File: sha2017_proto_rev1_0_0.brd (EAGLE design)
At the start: 95 x 46 mm, 1 part

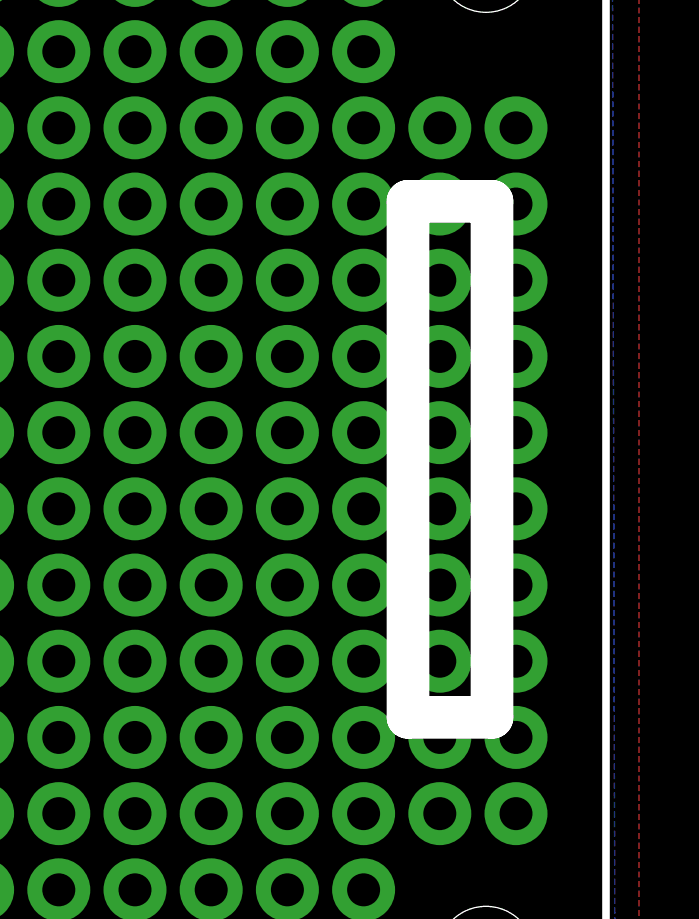
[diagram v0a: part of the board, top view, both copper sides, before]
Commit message: removed milling layer
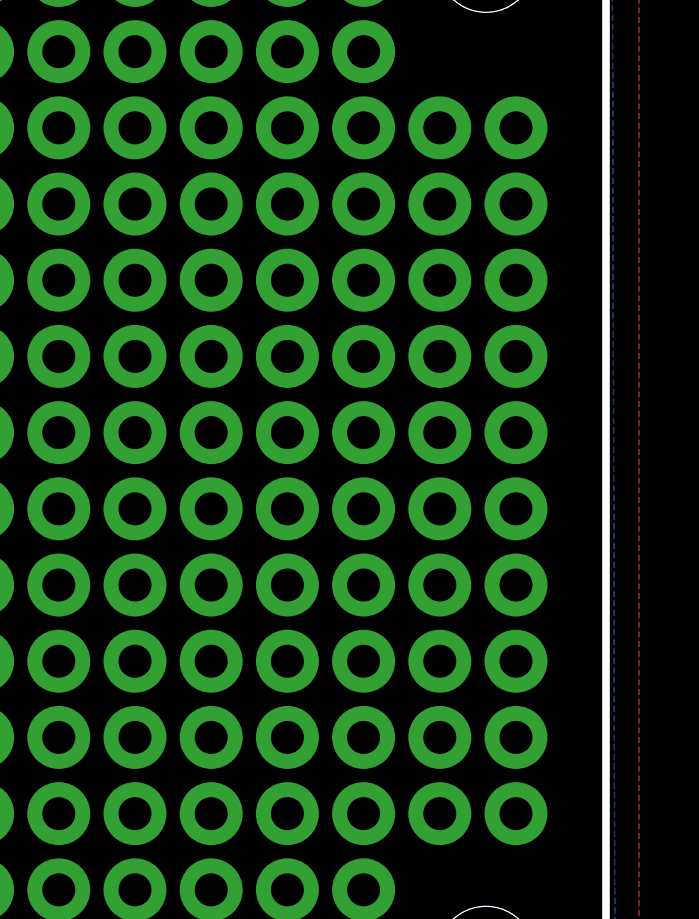
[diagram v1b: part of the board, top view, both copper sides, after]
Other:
- outline, holes or cut-outs redrawn
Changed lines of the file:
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@@
 <layer number="25" name="tNames" color="7" fill="1" visible="yes" active="yes"/>
 <layer number="26" name="bNames" color="7" fill="1" visible="yes" active="yes"/>
-<layer number="27" name="tValues" color="7" fill="1" visible="no" active="yes"/>
-<layer number="28" name="bValues" color="7" fill="1" visible="no" active="yes"/>
+<layer number="27" name="tValues" color="7" fill="1" visible="yes" active="yes"/>
+<layer number="28" name="bValues" color="7" fill="1" visible="yes" active="yes"/>
 <layer number="29" name="tStop" color="7" fill="3" visible="yes" active="yes"/>
 <layer number="30" name="bStop" color="7" fill="6" visible="yes" active="yes"/>
-<layer number="31" name="tCream" color="7" fill="4" visible="no" active="yes"/>
-<layer number="32" name="bCream" color="7" fill="5" visible="no" active="yes"/>
-<layer number="33" name="tFinish" color="6" fill="3" visible="no" active="yes"/>
-<layer number="34" name="bFinish" color="6" fill="6" visible="no" active="yes"/>
-<layer number="35" name="tGlue" color="7" fill="4" visible="no" active="yes"/>
-<layer number="36" name="bGlue" color="7" fill="5" visible="no" active="yes"/>
-<layer number="37" name="tTest" color="7" fill="1" visible="no" active="yes"/>
-<layer number="38" name="bTest" color="7" fill="1" visible="no" active="yes"/>
-<layer number="39" name="tKeepout" color="4" fill="11" visible="no" active="yes"/>
-<layer number="40" name="bKeepout" color="1" fill="11" visible="no" active="yes"/>
-<layer number="41" name="tRestrict" color="4" fill="10" visible="no" active="yes"/>
-<layer number="42" name="bRestrict" color="1" fill="10" visible="no" active="yes"/>
-<layer number="43" name="vRestrict" color="2" fill="10" visible="no" active="yes"/>
-<layer number="44" name="Drills" color="7" fill="1" visible="no" active="yes"/>
+<layer number="31" name="tCream" color="7" fill="4" visible="yes" active="yes"/>
+<layer number="32" name="bCream" color="7" fill="5" visible="yes" active="yes"/>
+<layer number="33" name="tFinish" color="6" fill="3" visible="yes" active="yes"/>
+<layer number="34" name="bFinish" color="6" fill="6" visible="yes" active="yes"/>
+<layer number="35" name="tGlue" color="7" fill="4" visible="yes" active="yes"/>
+<layer number="36" name="bGlue" color="7" fill="5" visible="yes" active="yes"/>
+<layer number="37" name="tTest" color="7" fill="1" visible="yes" active="yes"/>
+<layer number="38" name="bTest" color="7" fill="1" visible="yes" active="yes"/>
+<layer number="39" name="tKeepout" color="4" fill="11" visible="yes" active="yes"/>
+<layer number="40" name="bKeepout" color="1" fill="11" visible="yes" active="yes"/>
+<layer number="41" name="tRestrict" color="4" fill="10" visible="yes" active="yes"/>
+<layer number="42" name="bRestrict" color="1" fill="10" visible="yes" active="yes"/>
+<layer number="43" name="vRestrict" color="2" fill="10" visible="yes" active="yes"/>
+<layer number="44" name="Drills" color="7" fill="1" visible="yes" active="yes"/>
 <layer number="45" name="Holes" color="7" fill="1" visible="yes" active="yes"/>
-<layer number="46" name="Milling" color="3" fill="1" visible="no" active="yes"/>
-<layer number="47" name="Measures" color="7" fill="1" visible="no" active="yes"/>
-<layer number="48" name="Document" color="7" fill="1" visible="no" active="yes"/>
-<layer number="49" name="Reference" color="7" fill="1" visible="no" active="yes"/>
+<layer number="46" name="Milling" color="3" fill="1" visible="yes" active="yes"/>
+<layer number="47" name="Measures" color="7" fill="1" visible="yes" active="yes"/>
+<layer number="48" name="Document" color="7" fill="1" visible="yes" active="yes"/>
+<layer number="49" name="Reference" color="7" fill="1" visible="yes" active="yes"/>
 <layer number="50" name="dxf" color="7" fill="1" visible="no" active="no"/>
-<layer number="51" name="tDocu" color="7" fill="1" visible="no" active="yes"/>
-<layer number="52" name="bDocu" color="7" fill="1" visible="no" active="yes"/>
+<layer number="51" name="tDocu" color="7" fill="1" visible="yes" active="yes"/>
+<layer number="52" name="bDocu" color="7" fill="1" visible="yes" active="yes"/>
 <layer number="53" name="tGND_GNDA" color="7" fill="9" visible="no" active="no"/>
 <layer number="54" name="bGND_GNDA" color="1" fill="9" visible="no" active="no"/>
@@
 <layer number="60" name="bCarbon" color="7" fill="1" visible="no" active="no"/>
 <layer number="61" name="stand" color="7" fill="1" visible="no" active="no"/>
-<layer number="90" name="Modules" color="5" fill="1" visible="no" active="yes"/>
+<layer number="90" name="Modules" color="5" fill="1" visible="yes" active="yes"/>
 <layer number="91" name="Nets" color="2" fill="1" visible="no" active="no"/>
 <layer number="92" name="Busses" color="1" fill="1" visible="no" active="no"/>
@@
 <layer number="99" name="SpiceOrder" color="7" fill="1" visible="no" active="no"/>
 <layer number="100" name="Muster" color="7" fill="1" visible="no" active="no"/>
-<layer number="101" name="Patch_Top" color="12" fill="4" visible="no" active="yes"/>
-<layer number="102" name="Vscore" color="7" fill="1" visible="no" active="yes"/>
-<layer number="103" name="tMap" color="7" fill="1" visible="no" active="yes"/>
-<layer number="104" name="Name" color="16" fill="1" visible="no" active="yes"/>
-<layer number="105" name="tPlate" color="7" fill="1" visible="no" active="yes"/>
-<layer number="106" name="bPlate" color="7" fill="1" visible="no" active="yes"/>
-<layer number="107" name="Crop" color="7" fill="1" visible="no" active="yes"/>
-<layer number="108" name="tplace-old" color="10" fill="1" visible="no" active="yes"/>
-<layer number="109" name="ref-old" color="11" fill="1" visible="no" active="yes"/>
-<layer number="110" name="fp0" color="7" fill="1" visible="no" active="yes"/>
-<layer number="111" name="LPC17xx" color="7" fill="1" visible="no" active="yes"/>
-<layer number="112" name="tSilk" color="7" fill="1" visible="no" active="yes"/>
+<layer number="101" name="Patch_Top" color="12" fill="4" visible="yes" active="yes"/>
+<layer number="102" name="Vscore" color="7" fill="1" visible="yes" active="yes"/>
+<layer number="103" name="tMap" color="7" fill="1" visible="yes" active="yes"/>
+<layer number="104" name="Name" color="16" fill="1" visible="yes" active="yes"/>
+<layer number="105" name="tPlate" color="7" fill="1" visible="yes" active="yes"/>
+<layer number="106" name="bPlate" color="7" fill="1" visible="yes" active="yes"/>
+<layer number="107" name="Crop" color="7" fill="1" visible="yes" active="yes"/>
+<layer number="108" name="tplace-old" color="10" fill="1" visible="yes" active="yes"/>
+<layer number="109" name="ref-old" color="11" fill="1" visible="yes" active="yes"/>
+<layer number="110" name="fp0" color="7" fill="1" visible="yes" active="yes"/>
+<layer number="111" name="LPC17xx" color="7" fill="1" visible="yes" active="yes"/>
+<layer number="112" name="tSilk" color="7" fill="1" visible="yes" active="yes"/>
 <layer number="113" name="IDFDebug" color="7" fill="1" visible="no" active="yes"/>
 <layer number="116" name="Patch_BOT" color="9" fill="4" visible="no" active="yes"/>
@@
 <wire x1="95" y1="43" x2="95" y2="81" width="0.254" layer="20"/>
 <wire x1="95" y1="81" x2="91" y2="85" width="0.254" layer="20" curve="90"/>
-<wire x1="91.2" y1="67.1" x2="91.2" y2="49.9" width="1.4224" layer="46"/>
-<wire x1="91.2" y1="49.9" x2="88.4" y2="49.9" width="1.4224" layer="46"/>
-<wire x1="88.4" y1="49.9" x2="88.4" y2="67.1" width="1.4224" layer="46"/>
-<wire x1="88.4" y1="67.1" x2="91.2" y2="67.1" width="1.4224" layer="46"/>
 <hole x="3" y="57" drill="3.2"/>
 <hole x="91" y="42" drill="3.2"/>
@@
 <via x="86.92" y="67.01" extent="1-16" drill="1.1" diameter="2.1" shape="square" alwaysstop="yes"/>
 </signal>
+<signal name="N$1">
+<via x="89.46" y="67.01" extent="1-16" drill="1.1" diameter="2.1" shape="square" alwaysstop="yes"/>
+</signal>
 <signal name="N$371">
-<via x="89.46" y="67.01" extent="1-16" drill="1.1" diameter="2.1" shape="square" alwaysstop="yes"/>
 <via x="92" y="67.01" extent="1-16" drill="1.1" diameter="2.1" shape="square" alwaysstop="yes"/>
-<wire x1="89.46" y1="67.01" x2="92" y2="67.01" width="0" layer="19" extent="1-1"/>
 </signal>
 <signal name="N$374">
@@
 <via x="92" y="82.25" extent="1-16" drill="1.1" diameter="2.1" shape="square" alwaysstop="yes"/>
 <via x="89.46" y="82.25" extent="1-16" drill="1.1" diameter="2.1" shape="square" alwaysstop="yes"/>
+<wire x1="92" y1="79.71" x2="92" y2="82.25" width="0" layer="19" extent="1-1"/>
+<wire x1="89.46" y1="82.25" x2="92" y2="82.25" width="0" layer="19" extent="1-1"/>
+<wire x1="89.46" y1="79.71" x2="92" y2="79.71" width="0" layer="19" extent="1-1"/>
+<wire x1="86.92" y1="79.71" x2="89.46" y2="79.71" width="0" layer="19" extent="1-1"/>
 </signal>
 <signal name="N$544">

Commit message: criticial patch! mirror interface socket!
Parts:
- moved JP1 12.7 mm to (53.9, 51.7), flipped to the bottom
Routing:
- net 3V3_SWITCHED: track 7.71 -> 13.6 mm
- net I2C_SDA: track 10.6 -> 5.14 mm
- net GND: track 2.57 -> 0.00 mm, vias 4 -> 3
